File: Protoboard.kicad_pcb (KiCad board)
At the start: 2 copper layers, 90.5 x 90.5 mm, 60 parts, among them P1 CONN_01X08, P2 CONN_01X04, P3 CONN_01X05, P4 CONN_01X11, P5 CONN_02X05

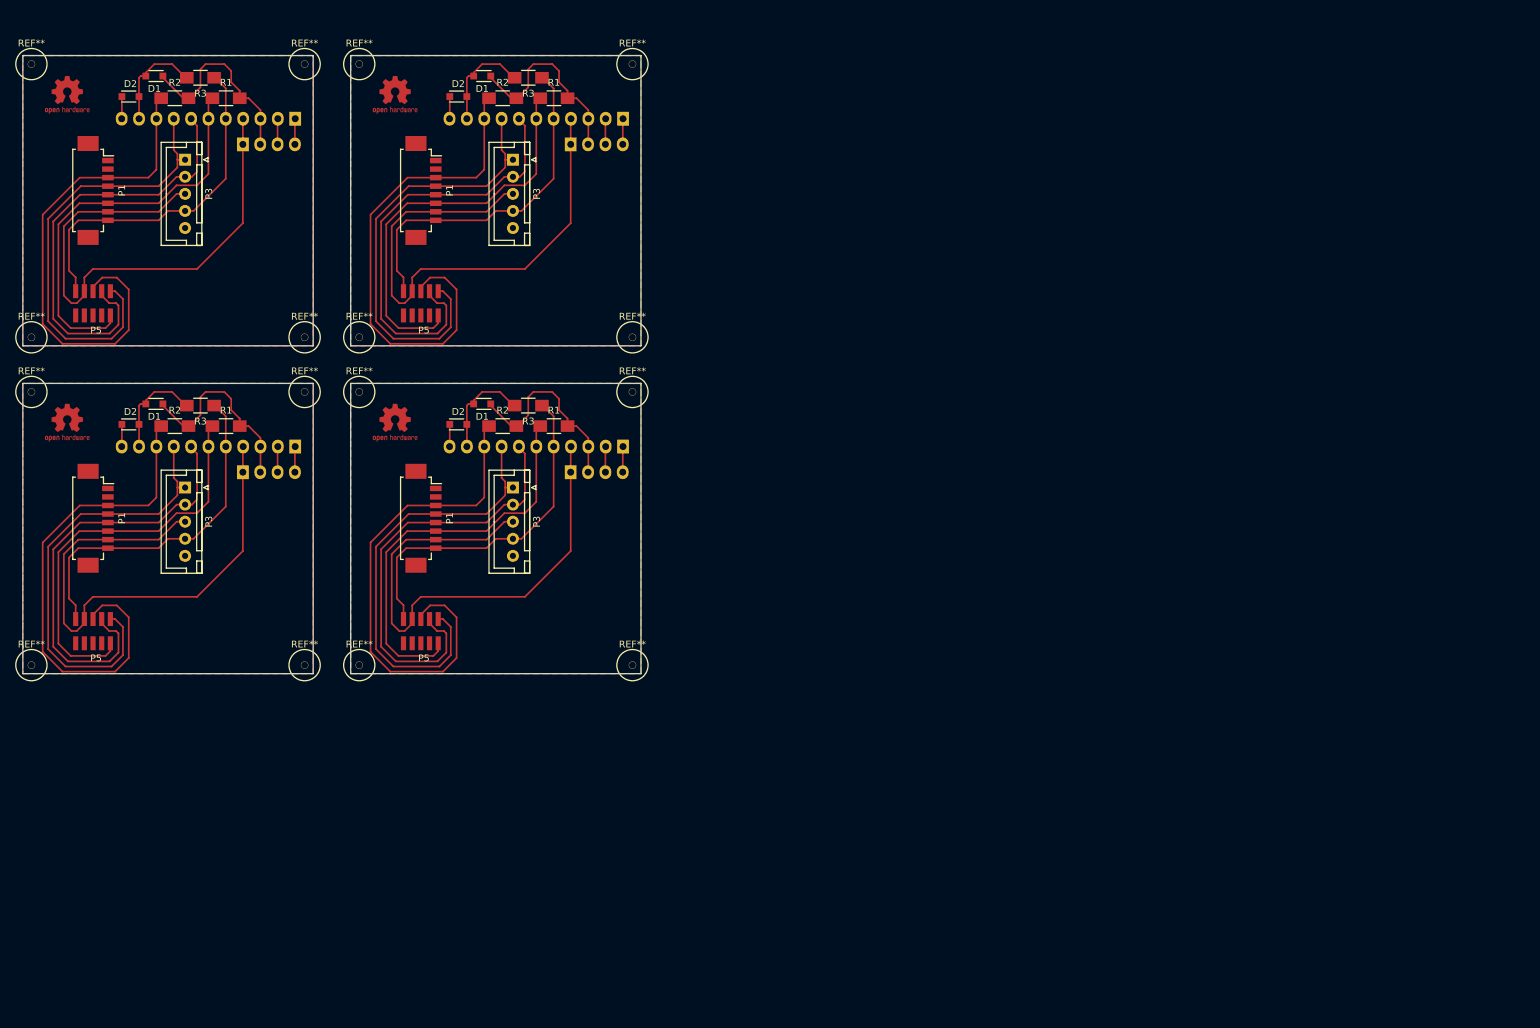
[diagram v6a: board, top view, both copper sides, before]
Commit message: Routing and fill zones.
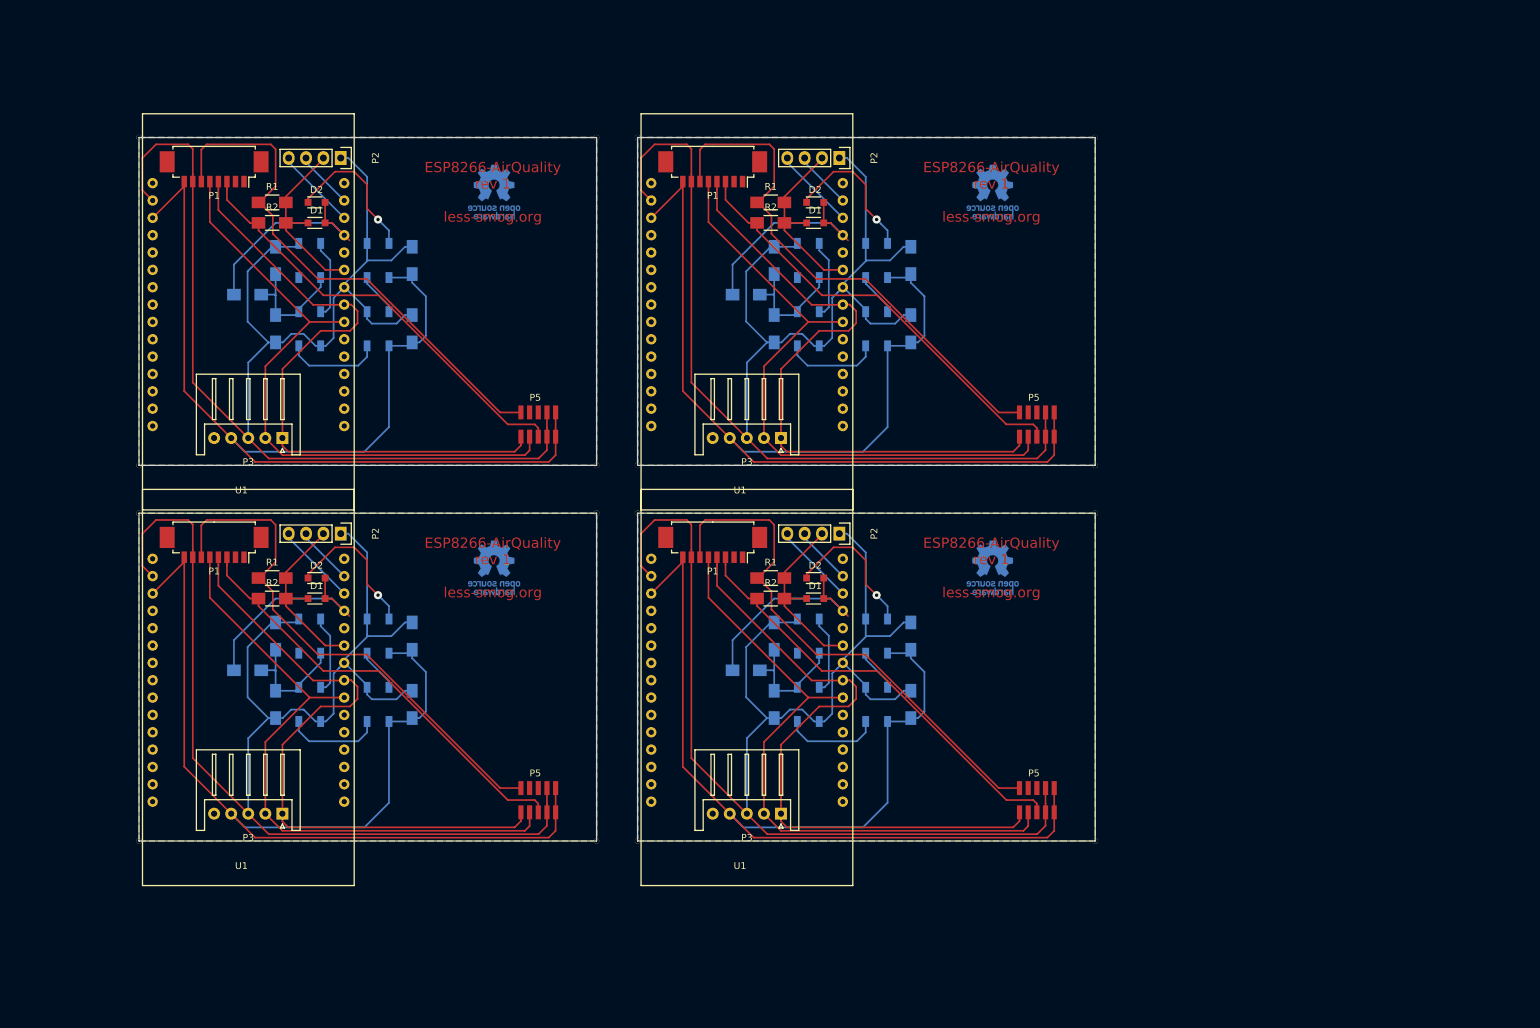
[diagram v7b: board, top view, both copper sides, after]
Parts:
- removed the D1 at (82.2, 71.0)
- removed the D1 at (82.2, 23.0)
- removed the D1 at (34.2, 71.0)
- removed the D1 at (34.2, 23.0)
- removed the D2 at (78.8, 74.0)
- removed the D2 at (78.8, 26.0)
- removed the D2 at (30.8, 74.0)
- removed the D2 at (30.8, 26.0)
- removed the P1 at (74.0, 87.8)
- removed the P1 at (74.0, 39.8)
- removed the P1 at (26.0, 87.8)
- removed the P1 at (26.0, 39.8)
- removed the P2 at (95.2, 81.0)
- removed the P2 at (95.2, 33.0)
- removed the P2 at (47.2, 81.0)
- removed the P2 at (47.2, 33.0)
- removed the P3 at (86.8, 83.2)
- removed the P3 at (86.8, 35.2)
- removed the P3 at (38.8, 83.2)
- removed the P3 at (38.8, 35.2)
- removed P4 (x4): CONN_01X11, Pin_Headers:Pin_Header_Straight_1x11
- removed the P5 at (70.7, 106.0)
- removed the P5 at (70.7, 58.0)
- removed the P5 at (22.7, 106.0)
- removed the P5 at (22.7, 58.0)
- removed the R1 at (92.8, 74.2)
- removed the R1 at (92.8, 26.2)
- removed the R1 at (44.8, 74.2)
- removed the R1 at (44.8, 26.2)
- removed the R2 at (85.2, 74.2)
- removed the R2 at (85.2, 26.2)
- removed the R2 at (37.2, 74.2)
- removed the R2 at (37.2, 26.2)
- removed the R3 at (89.0, 71.2)
- removed the R3 at (89.0, 23.2)
- removed the R3 at (41.0, 71.2)
- removed the R3 at (41.0, 23.2)
- removed REF** (x16): 1pin, Connectors:1pin
- removed the REF*** at (69.5, 73.8)
- removed the REF*** at (69.5, 25.8)
- removed the REF*** at (21.5, 73.8)
- removed the REF*** at (21.5, 25.8)
- added ?: , Wire_Pads:SolderWirePad_single_0-8mmDrill, F.Cu at (172.0, 135.0)
- added ?: , Wire_Pads:SolderWirePad_single_0-8mmDrill, F.Cu at (105.0, 87.0)
- added ?: , Wire_Pads:SolderWirePad_single_0-8mmDrill, F.Cu at (32.0, 87.0)
- added ?: , Wire_Pads:SolderWirePad_single_0-8mmDrill, F.Cu at (105.0, 32.0)
- added ?: , Wire_Pads:SolderWirePad_single_0-8mmDrill, F.Cu at (32.0, 32.0)
- added ?: , Wire_Pads:SolderWirePad_single_0-8mmDrill, F.Cu at (32.0, 80.0)
- added ?: , Wire_Pads:SolderWirePad_single_0-8mmDrill, F.Cu at (99.0, 80.0)
- added ?: , Wire_Pads:SolderWirePad_single_0-8mmDrill, F.Cu at (99.0, 32.0)
- added ?: , Wire_Pads:SolderWirePad_single_0-8mmDrill, F.Cu at (99.0, 135.0)
- added ?: , Wire_Pads:SolderWirePad_single_0-8mmDrill, F.Cu at (172.0, 80.0)
- added ?: , Wire_Pads:SolderWirePad_single_0-8mmDrill, F.Cu at (172.0, 87.0)
- added ?: , Wire_Pads:SolderWirePad_single_0-8mmDrill, F.Cu at (99.0, 87.0)
- added ?: , Wire_Pads:SolderWirePad_single_0-8mmDrill, F.Cu at (172.0, 32.0)
- added ?: , Wire_Pads:SolderWirePad_single_0-8mmDrill, F.Cu at (105.0, 135.0)
- added ?: , Wire_Pads:SolderWirePad_single_0-8mmDrill, F.Cu at (32.0, 135.0)
- added ?: , Wire_Pads:SolderWirePad_single_0-8mmDrill, F.Cu at (105.0, 80.0)
- added C1: 100nF, Capacitors_SMD:C_1206_HandSoldering, B.Cu at (145.0, 105.0)
- added C1: 100nF, Capacitors_SMD:C_1206_HandSoldering, B.Cu at (72.0, 105.0)
- added C1: 100nF, Capacitors_SMD:C_1206_HandSoldering, B.Cu at (145.0, 50.0)
- added C1: 100nF, Capacitors_SMD:C_1206_HandSoldering, B.Cu at (72.0, 50.0)
- added C2: 100nF, Capacitors_SMD:C_1206_HandSoldering, B.Cu at (145.0, 115.0)
- added C2: 100nF, Capacitors_SMD:C_1206_HandSoldering, B.Cu at (72.0, 115.0)
- added C2: 100nF, Capacitors_SMD:C_1206_HandSoldering, B.Cu at (145.0, 60.0)
- added C2: 100nF, Capacitors_SMD:C_1206_HandSoldering, B.Cu at (72.0, 60.0)
- added C3: 100nF, Capacitors_SMD:C_1206_HandSoldering, B.Cu at (125.0, 115.0)
- added C3: 100nF, Capacitors_SMD:C_1206_HandSoldering, B.Cu at (52.0, 115.0)
- added C3: 100nF, Capacitors_SMD:C_1206_HandSoldering, B.Cu at (125.0, 60.0)
- added C3: 100nF, Capacitors_SMD:C_1206_HandSoldering, B.Cu at (52.0, 60.0)
- added C4: 100nF, Capacitors_SMD:C_1206_HandSoldering, B.Cu at (125.0, 105.0)
- added C4: 100nF, Capacitors_SMD:C_1206_HandSoldering, B.Cu at (52.0, 105.0)
- added C4: 100nF, Capacitors_SMD:C_1206_HandSoldering, B.Cu at (125.0, 50.0)
- added C4: 100nF, Capacitors_SMD:C_1206_HandSoldering, B.Cu at (52.0, 50.0)
- added D1: D, Diodes_SMD:SOD-323_HandSoldering, F.Cu at (131.0, 99.5)
- added D1: D, Diodes_SMD:SOD-323_HandSoldering, F.Cu at (58.0, 99.5)
- added D1: D, Diodes_SMD:SOD-323_HandSoldering, F.Cu at (131.0, 44.5)
- added D1: D, Diodes_SMD:SOD-323_HandSoldering, F.Cu at (58.0, 44.5)
- added D2: D, Diodes_SMD:SOD-323_HandSoldering, F.Cu at (131.0, 96.5)
- added D2: D, Diodes_SMD:SOD-323_HandSoldering, F.Cu at (58.0, 96.5)
- added D2: D, Diodes_SMD:SOD-323_HandSoldering, F.Cu at (131.0, 41.5)
- added D2: D, Diodes_SMD:SOD-323_HandSoldering, F.Cu at (58.0, 41.5)
- added LED1: WS2812B, LEDs:LED_WS2812B-PLCC4, B.Cu at (140.0, 105.0)
- added LED1: WS2812B, LEDs:LED_WS2812B-PLCC4, B.Cu at (67.0, 105.0)
- added LED1: WS2812B, LEDs:LED_WS2812B-PLCC4, B.Cu at (140.0, 50.0)
- added LED1: WS2812B, LEDs:LED_WS2812B-PLCC4, B.Cu at (67.0, 50.0)
- added LED2: WS2812B, LEDs:LED_WS2812B-PLCC4, B.Cu at (140.0, 115.0)
- added LED2: WS2812B, LEDs:LED_WS2812B-PLCC4, B.Cu at (67.0, 115.0)
- added LED2: WS2812B, LEDs:LED_WS2812B-PLCC4, B.Cu at (140.0, 60.0)
- added LED2: WS2812B, LEDs:LED_WS2812B-PLCC4, B.Cu at (67.0, 60.0)
- added LED3: WS2812B, LEDs:LED_WS2812B-PLCC4, B.Cu at (130.0, 115.0)
- added LED3: WS2812B, LEDs:LED_WS2812B-PLCC4, B.Cu at (57.0, 115.0)
- added LED3: WS2812B, LEDs:LED_WS2812B-PLCC4, B.Cu at (130.0, 60.0)
- added LED3: WS2812B, LEDs:LED_WS2812B-PLCC4, B.Cu at (57.0, 60.0)
- added LED4: WS2812B, LEDs:LED_WS2812B-PLCC4, B.Cu at (130.0, 105.0)
- added LED4: WS2812B, LEDs:LED_WS2812B-PLCC4, B.Cu at (57.0, 105.0)
- added LED4: WS2812B, LEDs:LED_WS2812B-PLCC4, B.Cu at (130.0, 50.0)
- added LED4: WS2812B, LEDs:LED_WS2812B-PLCC4, B.Cu at (57.0, 50.0)
- added P1: CONN_01X08, Connectors_Molex:Molex_PicoBlade_53261-0871_08x1.25mm_Angled, F.Cu at (116.0, 92.0)
- added P1: CONN_01X08, Connectors_Molex:Molex_PicoBlade_53261-0871_08x1.25mm_Angled, F.Cu at (43.0, 92.0)
- added P1: CONN_01X08, Connectors_Molex:Molex_PicoBlade_53261-0871_08x1.25mm_Angled, F.Cu at (116.0, 37.0)
- added P1: CONN_01X08, Connectors_Molex:Molex_PicoBlade_53261-0871_08x1.25mm_Angled, F.Cu at (43.0, 37.0)
- added P2: CONN_01X04, Pin_Headers:Pin_Header_Straight_1x04, F.Cu at (134.5, 90.0)
- added P2: CONN_01X04, Pin_Headers:Pin_Header_Straight_1x04, F.Cu at (61.5, 90.0)
- added P2: CONN_01X04, Pin_Headers:Pin_Header_Straight_1x04, F.Cu at (134.5, 35.0)
- added P2: CONN_01X04, Pin_Headers:Pin_Header_Straight_1x04, F.Cu at (61.5, 35.0)
- added P3: CONN_01X05, Connectors_JST:JST_XH_S05B-XH-A_05x2.50mm_Angled, F.Cu at (126.0, 131.0)
- added P3: CONN_01X05, Connectors_JST:JST_XH_S05B-XH-A_05x2.50mm_Angled, F.Cu at (53.0, 131.0)
- added P3: CONN_01X05, Connectors_JST:JST_XH_S05B-XH-A_05x2.50mm_Angled, F.Cu at (126.0, 76.0)
- added P3: CONN_01X05, Connectors_JST:JST_XH_S05B-XH-A_05x2.50mm_Angled, F.Cu at (53.0, 76.0)
- added P5: CONN_02X05, Amphenol:Amphenol, F.Cu at (166.0, 127.2)
- added P5: CONN_02X05, Amphenol:Amphenol, F.Cu at (93.0, 127.2)
- added P5: CONN_02X05, Amphenol:Amphenol, F.Cu at (166.0, 72.2)
- added P5: CONN_02X05, Amphenol:Amphenol, F.Cu at (93.0, 72.2)
- added R1: 10k, Resistors_SMD:R_1206_HandSoldering, F.Cu at (124.5, 96.5)
- added R1: 10k, Resistors_SMD:R_1206_HandSoldering, F.Cu at (51.5, 96.5)
- added R1: 10k, Resistors_SMD:R_1206_HandSoldering, F.Cu at (124.5, 41.5)
- added R1: 10k, Resistors_SMD:R_1206_HandSoldering, F.Cu at (51.5, 41.5)
- added R2: 10k, Resistors_SMD:R_1206_HandSoldering, F.Cu at (124.5, 99.5)
- added R2: 10k, Resistors_SMD:R_1206_HandSoldering, F.Cu at (51.5, 99.5)
- added R2: 10k, Resistors_SMD:R_1206_HandSoldering, F.Cu at (124.5, 44.5)
- added R2: 10k, Resistors_SMD:R_1206_HandSoldering, F.Cu at (51.5, 44.5)
- added R3: 10k, Resistors_SMD:R_1206_HandSoldering, B.Cu at (120.9, 110.0)
- added R3: 10k, Resistors_SMD:R_1206_HandSoldering, B.Cu at (47.9, 110.0)
- added R3: 10k, Resistors_SMD:R_1206_HandSoldering, B.Cu at (120.9, 55.0)
- added R3: 10k, Resistors_SMD:R_1206_HandSoldering, B.Cu at (47.9, 55.0)
- added REF***: OSHW-Logo_7.5x8mm_Copper, Symbols:OSHW-Logo_7.5x8mm_Copper, B.Cu at (157.0, 95.0)
- added REF***: OSHW-Logo_7.5x8mm_Copper, Symbols:OSHW-Logo_7.5x8mm_Copper, B.Cu at (84.0, 95.0)
- added REF***: OSHW-Logo_7.5x8mm_Copper, Symbols:OSHW-Logo_7.5x8mm_Copper, B.Cu at (157.0, 40.0)
- added REF***: OSHW-Logo_7.5x8mm_Copper, Symbols:OSHW-Logo_7.5x8mm_Copper, B.Cu at (84.0, 40.0)
- added U1: LoLin_V3, LoLin:LoLin, F.Cu at (105.3, 83.5)
- added U1: LoLin_V3, LoLin:LoLin, F.Cu at (32.3, 83.5)
- added U1: LoLin_V3, LoLin:LoLin, F.Cu at (105.3, 28.5)
- added U1: LoLin_V3, LoLin:LoLin, F.Cu at (32.3, 28.5)
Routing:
- net GND: track 318.1 -> 843.5 mm
- net +5V: track 204.1 -> 712.5 mm
- net RXD: track 255.7 -> 373.5 mm
- net TXD: track 261.0 -> 377.8 mm
- net LED: track 13.0 -> 86.2 mm, vias 0 -> 4
- net SET: track 238.1 -> 310.6 mm
- net DIN: track 61.3 -> 127.8 mm
- net Net-(LED2-Pad2): track 0.00 -> 56.6 mm
- net Net-(LED3-Pad2): track 0.00 -> 46.4 mm
- net RESET: track 295.5 -> 256.1 mm
- net SCL: track 15.1 -> 48.5 mm
- net Net-(LED1-Pad2): track 0.00 -> 25.3 mm
- net SDA: track 15.1 -> 34.1 mm
- net +3.3V: track 115.4 -> 111.1 mm
- added copper zone on B.Cu, net GND
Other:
- board size 90.5 x 90.5 mm -> 140 x 103 mm
- board text added: "ESP8266-AirQuality rev 1 less-smog.org"

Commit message: Moved PMS7003 connector 4mm towards the edge and regenerated all fab artifacts.
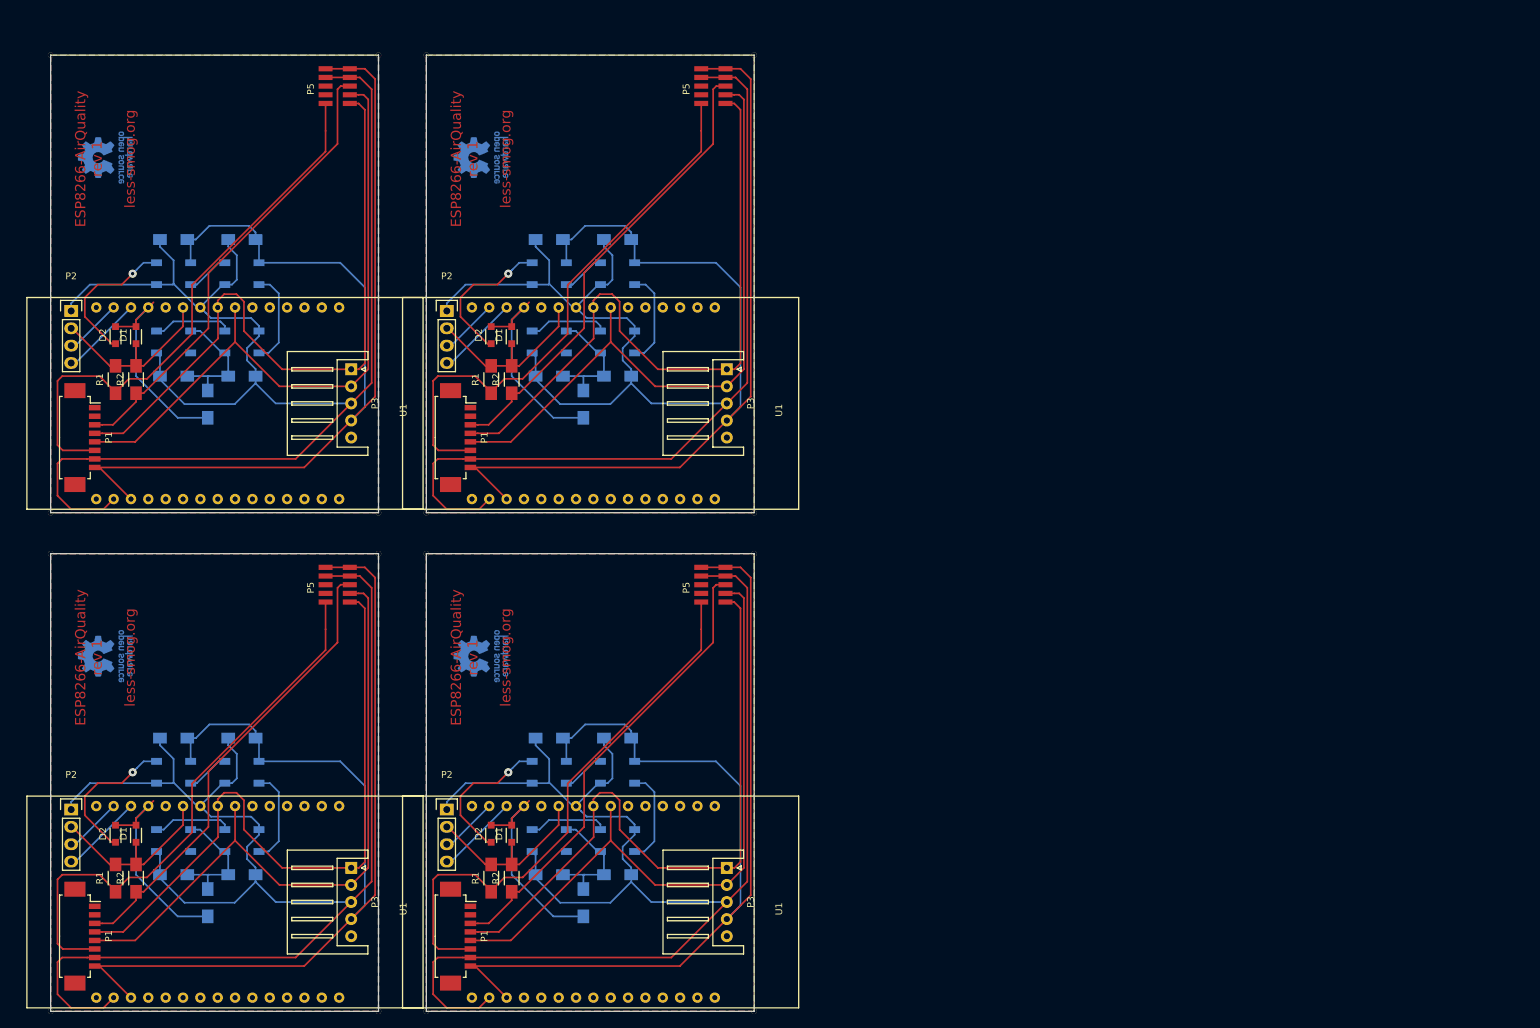
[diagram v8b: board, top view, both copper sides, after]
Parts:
- removed the ? at (172.0, 135.0)
- removed the ? at (105.0, 87.0)
- removed the ? at (32.0, 87.0)
- removed the ? at (105.0, 32.0)
- removed the ? at (99.0, 135.0)
- removed the ? at (172.0, 80.0)
- removed the ? at (172.0, 87.0)
- removed the ? at (99.0, 87.0)
- removed the ? at (172.0, 32.0)
- removed the ? at (105.0, 135.0)
- removed the ? at (32.0, 135.0)
- removed the ? at (105.0, 80.0)
- removed the C1 at (145.0, 105.0)
- removed the C1 at (72.0, 105.0)
- removed the C1 at (145.0, 50.0)
- removed the C2 at (145.0, 115.0)
- removed the C2 at (72.0, 115.0)
- removed the C2 at (145.0, 60.0)
- removed the C3 at (125.0, 115.0)
- removed the C3 at (52.0, 115.0)
- removed the C3 at (125.0, 60.0)
- removed the C4 at (125.0, 105.0)
- removed the C4 at (52.0, 105.0)
- removed the C4 at (125.0, 50.0)
- removed the D1 at (131.0, 99.5)
- removed the D1 at (58.0, 99.5)
- removed the D1 at (131.0, 44.5)
- removed the D2 at (131.0, 96.5)
- removed the D2 at (58.0, 96.5)
- removed the D2 at (131.0, 41.5)
- removed the LED1 at (140.0, 105.0)
- removed the LED1 at (67.0, 105.0)
- removed the LED1 at (140.0, 50.0)
- removed the LED2 at (140.0, 115.0)
- removed the LED2 at (67.0, 115.0)
- removed the LED2 at (140.0, 60.0)
- removed the LED3 at (130.0, 115.0)
- removed the LED3 at (57.0, 115.0)
- removed the LED3 at (130.0, 60.0)
- removed the LED4 at (130.0, 105.0)
- removed the LED4 at (57.0, 105.0)
- removed the LED4 at (130.0, 50.0)
- removed the P1 at (116.0, 92.0)
- removed the P1 at (43.0, 92.0)
- removed the P1 at (116.0, 37.0)
- removed the P2 at (134.5, 90.0)
- removed the P2 at (61.5, 90.0)
- removed the P2 at (134.5, 35.0)
- removed the P3 at (126.0, 131.0)
- removed the P3 at (53.0, 131.0)
- removed the P3 at (126.0, 76.0)
- removed the P5 at (166.0, 127.2)
- removed the P5 at (93.0, 127.2)
- removed the P5 at (166.0, 72.2)
- removed the R1 at (124.5, 96.5)
- removed the R1 at (51.5, 96.5)
- removed the R1 at (124.5, 41.5)
- removed the R2 at (124.5, 99.5)
- removed the R2 at (51.5, 99.5)
- removed the R2 at (124.5, 44.5)
- removed the R3 at (120.9, 110.0)
- removed the R3 at (47.9, 110.0)
- removed the R3 at (120.9, 55.0)
- removed the REF*** at (157.0, 95.0)
- removed the REF*** at (84.0, 95.0)
- removed the REF*** at (157.0, 40.0)
- removed the U1 at (105.3, 83.5)
- removed the U1 at (32.3, 83.5)
- removed the U1 at (105.3, 28.5)
- added ?: , Wire_Pads:SolderWirePad_single_0-8mmDrill, F.Cu at (74.1, 19.9)
- added ?: , Wire_Pads:SolderWirePad_single_0-8mmDrill, F.Cu at (74.1, 86.9)
- added ?: , Wire_Pads:SolderWirePad_single_0-8mmDrill, F.Cu at (74.1, 159.9)
- added ?: , Wire_Pads:SolderWirePad_single_0-8mmDrill, F.Cu at (19.1, 86.9)
- added ?: , Wire_Pads:SolderWirePad_single_0-8mmDrill, F.Cu at (74.1, 92.9)
- added ?: , Wire_Pads:SolderWirePad_single_0-8mmDrill, F.Cu at (19.1, 19.9)
- added ?: , Wire_Pads:SolderWirePad_single_0-8mmDrill, F.Cu at (122.1, 19.9)
- added ?: , Wire_Pads:SolderWirePad_single_0-8mmDrill, F.Cu at (122.1, 92.9)
- added ?: , Wire_Pads:SolderWirePad_single_0-8mmDrill, F.Cu at (67.1, 19.9)
- added ?: , Wire_Pads:SolderWirePad_single_0-8mmDrill, F.Cu at (122.1, 86.9)
- added ?: , Wire_Pads:SolderWirePad_single_0-8mmDrill, F.Cu at (122.1, 159.9)
- added ?: , Wire_Pads:SolderWirePad_single_0-8mmDrill, F.Cu at (67.1, 86.9)
- added C1: 100nF, Capacitors_SMD:C_1206_HandSoldering, B.Cu at (92.1, 46.9)
- added C1: 100nF, Capacitors_SMD:C_1206_HandSoldering, B.Cu at (92.1, 119.9)
- added C1: 100nF, Capacitors_SMD:C_1206_HandSoldering, B.Cu at (37.1, 46.9)
- added C2: 100nF, Capacitors_SMD:C_1206_HandSoldering, B.Cu at (102.1, 46.9)
- added C2: 100nF, Capacitors_SMD:C_1206_HandSoldering, B.Cu at (102.1, 119.9)
- added C2: 100nF, Capacitors_SMD:C_1206_HandSoldering, B.Cu at (47.1, 46.9)
- added C3: 100nF, Capacitors_SMD:C_1206_HandSoldering, B.Cu at (102.1, 66.9)
- added C3: 100nF, Capacitors_SMD:C_1206_HandSoldering, B.Cu at (102.1, 139.9)
- added C3: 100nF, Capacitors_SMD:C_1206_HandSoldering, B.Cu at (47.1, 66.9)
- added C4: 100nF, Capacitors_SMD:C_1206_HandSoldering, B.Cu at (92.1, 66.9)
- added C4: 100nF, Capacitors_SMD:C_1206_HandSoldering, B.Cu at (92.1, 139.9)
- added C4: 100nF, Capacitors_SMD:C_1206_HandSoldering, B.Cu at (37.1, 66.9)
- added D1: D, Diodes_SMD:SOD-323_HandSoldering, F.Cu at (86.6, 60.9)
- added D1: D, Diodes_SMD:SOD-323_HandSoldering, F.Cu at (86.6, 133.9)
- added D1: D, Diodes_SMD:SOD-323_HandSoldering, F.Cu at (31.6, 60.9)
- added D2: D, Diodes_SMD:SOD-323_HandSoldering, F.Cu at (83.6, 60.9)
- added D2: D, Diodes_SMD:SOD-323_HandSoldering, F.Cu at (83.6, 133.9)
- added D2: D, Diodes_SMD:SOD-323_HandSoldering, F.Cu at (28.6, 60.9)
- added LED1: WS2812B, LEDs:LED_WS2812B-PLCC4, B.Cu at (92.1, 51.9)
- added LED1: WS2812B, LEDs:LED_WS2812B-PLCC4, B.Cu at (92.1, 124.9)
- added LED1: WS2812B, LEDs:LED_WS2812B-PLCC4, B.Cu at (37.1, 51.9)
- added LED2: WS2812B, LEDs:LED_WS2812B-PLCC4, B.Cu at (102.1, 51.9)
- added LED2: WS2812B, LEDs:LED_WS2812B-PLCC4, B.Cu at (102.1, 124.9)
- added LED2: WS2812B, LEDs:LED_WS2812B-PLCC4, B.Cu at (47.1, 51.9)
- added LED3: WS2812B, LEDs:LED_WS2812B-PLCC4, B.Cu at (102.1, 61.9)
- added LED3: WS2812B, LEDs:LED_WS2812B-PLCC4, B.Cu at (102.1, 134.9)
- added LED3: WS2812B, LEDs:LED_WS2812B-PLCC4, B.Cu at (47.1, 61.9)
- added LED4: WS2812B, LEDs:LED_WS2812B-PLCC4, B.Cu at (92.1, 61.9)
- added LED4: WS2812B, LEDs:LED_WS2812B-PLCC4, B.Cu at (92.1, 134.9)
- added LED4: WS2812B, LEDs:LED_WS2812B-PLCC4, B.Cu at (37.1, 61.9)
- added P1: CONN_01X08, Connectors_Molex:Molex_PicoBlade_53261-0871_08x1.25mm_Angled, F.Cu at (79.1, 75.9)
- added P1: CONN_01X08, Connectors_Molex:Molex_PicoBlade_53261-0871_08x1.25mm_Angled, F.Cu at (79.1, 148.9)
- added P1: CONN_01X08, Connectors_Molex:Molex_PicoBlade_53261-0871_08x1.25mm_Angled, F.Cu at (24.1, 75.9)
- added P2: CONN_01X04, Pin_Headers:Pin_Header_Straight_1x04, F.Cu at (77.1, 57.4)
- added P2: CONN_01X04, Pin_Headers:Pin_Header_Straight_1x04, F.Cu at (77.1, 130.4)
- added P2: CONN_01X04, Pin_Headers:Pin_Header_Straight_1x04, F.Cu at (22.1, 57.4)
- added P3: CONN_01X05, Connectors_JST:JST_XH_S05B-XH-A_05x2.50mm_Angled, F.Cu at (118.1, 65.9)
- added P3: CONN_01X05, Connectors_JST:JST_XH_S05B-XH-A_05x2.50mm_Angled, F.Cu at (118.1, 138.9)
- added P3: CONN_01X05, Connectors_JST:JST_XH_S05B-XH-A_05x2.50mm_Angled, F.Cu at (63.1, 65.9)
- added P5: CONN_02X05, Amphenol:Amphenol, F.Cu at (114.3, 21.9)
- added P5: CONN_02X05, Amphenol:Amphenol, F.Cu at (114.3, 94.9)
- added P5: CONN_02X05, Amphenol:Amphenol, F.Cu at (59.3, 21.9)
- added R1: 10k, Resistors_SMD:R_1206_HandSoldering, F.Cu at (83.6, 67.4)
- added R1: 10k, Resistors_SMD:R_1206_HandSoldering, F.Cu at (83.6, 140.4)
- added R1: 10k, Resistors_SMD:R_1206_HandSoldering, F.Cu at (28.6, 67.4)
- added R2: 10k, Resistors_SMD:R_1206_HandSoldering, F.Cu at (86.6, 67.4)
- added R2: 10k, Resistors_SMD:R_1206_HandSoldering, F.Cu at (86.6, 140.4)
- added R2: 10k, Resistors_SMD:R_1206_HandSoldering, F.Cu at (31.6, 67.4)
- added R3: 10k, Resistors_SMD:R_1206_HandSoldering, B.Cu at (97.1, 71.0)
- added R3: 10k, Resistors_SMD:R_1206_HandSoldering, B.Cu at (97.1, 144.0)
- added R3: 10k, Resistors_SMD:R_1206_HandSoldering, B.Cu at (42.1, 71.0)
- added REF***: OSHW-Logo_7.5x8mm_Copper, Symbols:OSHW-Logo_7.5x8mm_Copper, B.Cu at (82.1, 34.9)
- added REF***: OSHW-Logo_7.5x8mm_Copper, Symbols:OSHW-Logo_7.5x8mm_Copper, B.Cu at (82.1, 107.9)
- added REF***: OSHW-Logo_7.5x8mm_Copper, Symbols:OSHW-Logo_7.5x8mm_Copper, B.Cu at (27.1, 34.9)
- added U1: LoLin_V3, LoLin:LoLin, F.Cu at (70.6, 86.7)
- added U1: LoLin_V3, LoLin:LoLin, F.Cu at (70.6, 159.7)
- added U1: LoLin_V3, LoLin:LoLin, F.Cu at (15.6, 86.7)
- moved U1 132.2 mm to (15.6, 159.7), turned to 90 degrees
- moved ? 128.6 mm to (19.1, 159.9), turned to 90 degrees
- moved P1 113.5 mm to (24.1, 148.9), turned to 270 degrees
- moved P2 103.2 mm to (22.1, 130.4), turned to 0 degrees
- moved R1 101.6 mm to (28.6, 140.4), turned to 90 degrees
- moved ? 100.5 mm to (19.1, 92.9), turned to 90 degrees
- moved R2 98.0 mm to (31.6, 140.4), turned to 90 degrees
- moved D2 97.0 mm to (28.6, 133.9), turned to 90 degrees
- moved D1 93.3 mm to (31.6, 133.9), turned to 90 degrees
- moved C4 91.2 mm to (37.1, 139.9), turned to 0 degrees
- moved R3 89.2 mm to (42.1, 144.0), turned to 270 degrees
- moved REF*** 88.6 mm to (27.1, 107.9), turned to 270 degrees
- moved ? 87.3 mm to (67.1, 159.9), turned to 90 degrees
- moved LED4 87.2 mm to (37.1, 134.9), turned to 180 degrees
- moved LED1 80.7 mm to (37.1, 124.9), turned to 180 degrees
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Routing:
- net RESET: track 256.1 -> 272.2 mm
- net TXD: track 377.8 -> 393.8 mm
- net RXD: track 373.5 -> 389.5 mm
- net SET: track 310.6 -> 326.6 mm
- net +5V: track 712.5 -> 727.3 mm
- net GND: track 843.5 -> 858.3 mm
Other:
- board size 140 x 103 mm -> 103 x 140 mm
